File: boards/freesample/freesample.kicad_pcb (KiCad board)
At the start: 8 copper layers, 576 parts, among them J1 SMA, J10 XILINX_JTAG, J11 SMA, J12 SMA, J13 SMA, J14 SMA, J15 SMA, J16 SMA, J17 SMA, J18 SMA, J19 JUMPER, J2 BARREL, J20 JUMPER, J21 JUMPER, J22 SMA, J23 SMA, J24 SMA, J25 SMA, J26 PMOD_HOST, J3 SMA, J4 SMA, J5 SMA, J6 XILINX_JTAG, J7 CONN_INTEGRALSTICK_FPGA_HOST, J8 CONN_INTEGRALSTICK_MCU_HOST, J9 0826-1G1T-23-F, M1 TRACEPAD, M2 LOGO1, M3 LOGO2, M4 LOGO3, M5 LOGO4, M6 LOGO5, M7 LOGO6, Q1 SSM6N58NU, U1 HMC675LP3E, U10 PI6C59S6005, U11 PI6C59S6005, U12 PI6C59S6005, U13 SIP32408, U14 LMK04806, U15 ASG-D-V-A-125.000MHZ, U16 HMC856, U17 NB6L295, U18 PI6C59S6005, U19 NB7V52MMNG, U2 HMC675LP3E, U20 NB7V52MMNG, U21 NB7V52MMNG, U22 PI6C59S6005, U26 MCP1755ST-5002E/MC, U27 LM27761, U28 ADP1763Z-1.0, U29 ADP1763Z-1.0, U3 PI6C59S6005, U30 OKL-T/3-W12P-C, U31 ADP1741, U32 OKL-T/3-W12P-C, U33 ADP1741, U34 ADP1741, U35 OKL-T/3-W12P-C, U36 OKL-T/3-W12P-C, U37 LM27761, U38 OKL-T/3-W12P-C, U39 LM27761, U4 LTC2664CUH-16#PBF, U40 DS25BR150, U41 DS25BR150, U42 ADP1741, U43 ADP1741, U5 TLK10232, U6 LMK61PD0A2, U7 PI6C59S6005, U8 HMC675LP3E, U9 HMC675LP3E

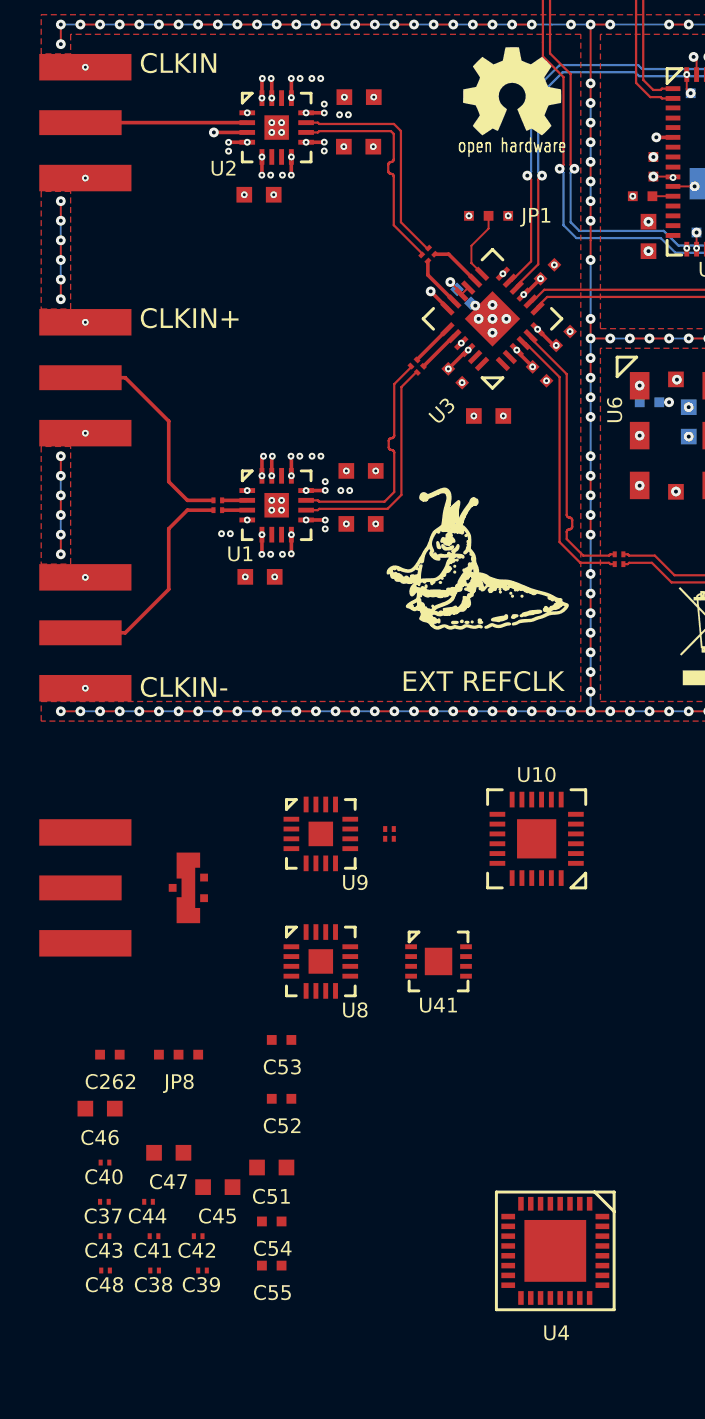
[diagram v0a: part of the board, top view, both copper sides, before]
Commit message: Continued layout on level trigger subsystem
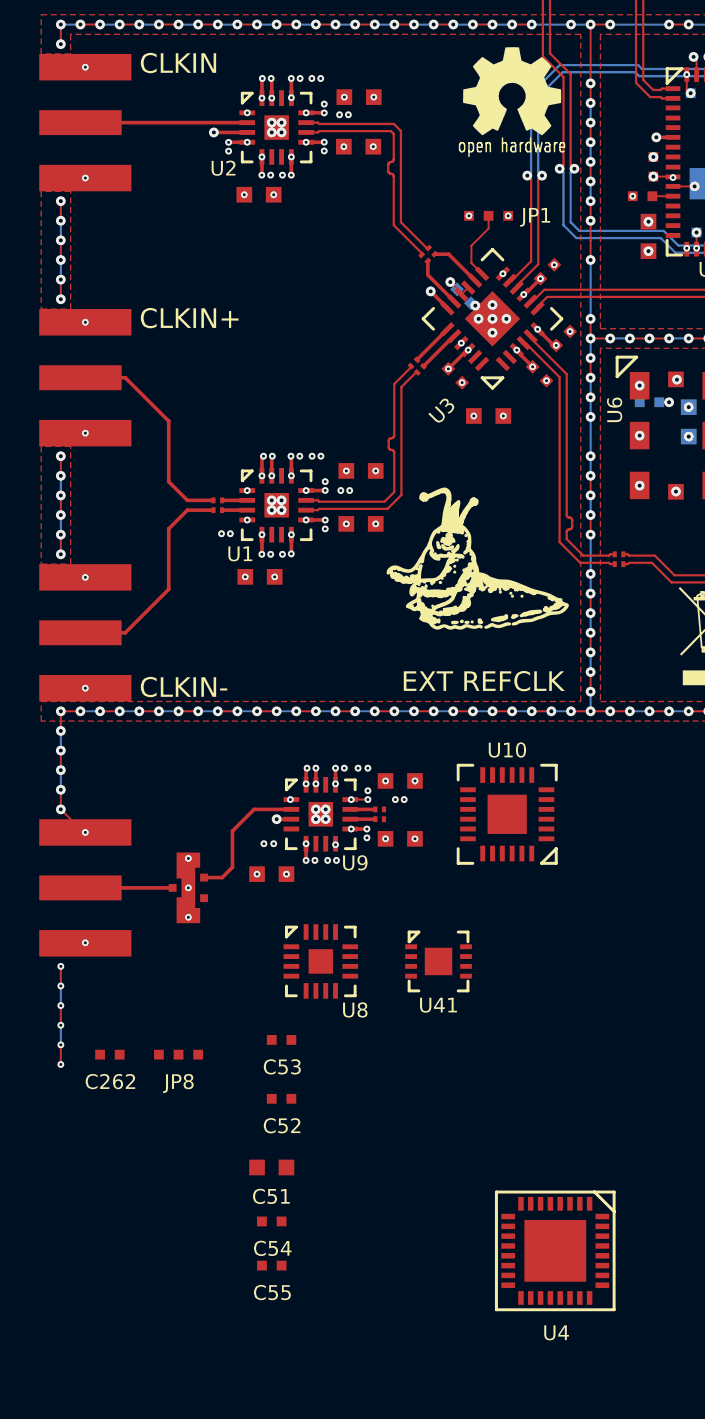
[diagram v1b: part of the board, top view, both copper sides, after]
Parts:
- moved C48 27.7 mm to (29.8, 157.9)
- moved C38 26.5 mm to (32.6, 159.3), turned to 90 degrees
- moved C39 26.5 mm to (31.2, 157.9)
- moved C42 25.3 mm to (32.4, 157.9)
- moved C44 24.2 mm to (34.3, 159.5)
- moved C41 23.2 mm to (32.6, 161.2), turned to 270 degrees
- moved C45 22.7 mm to (34.3, 158.6)
- moved C43 22.4 mm to (30.8, 162.6)
- moved C37 20.1 mm to (27.6, 161.8), turned to 180 degrees
- moved C47 19.9 mm to (34.3, 161.5)
- moved C40 18.6 mm to (29.7, 162.6)
- moved C46 14.8 mm to (27.8, 163.3)
- moved U10 1.95 mm to (39.8, 160.2)
- moved C49 1.12 mm to (33.2, 160.0), turned to 180 degrees
- moved C50 1.12 mm to (33.2, 160.5), turned to 180 degrees
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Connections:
- U10 pad 23: /Level triggering/LTRIG_SAMPOUT_N -> (no net)
- U10 pad 24: /Level triggering/LTRIG_SAMPOUT_P -> (no net)
- U10 pad 4: (no net) -> /Level triggering/LTRIG_SAMPOUT_N
- U10 pad 5: (no net) -> /Level triggering/LTRIG_SAMPOUT_P
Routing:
- net /GND: track 565.4 -> 632.0 mm, vias 369 -> 400
- net /1V8: track 91.1 -> 141.5 mm, vias 23 -> 29
- net /REFCLK_SINGLE_VT: track 33.8 -> 52.6 mm
- net /LTRIG_VT: track 0.00 -> 18.0 mm, vias 0 -> 1
- net /3V3: track 46.6 -> 63.7 mm, vias 14 -> 21
- net /3V0_N: track 48.1 -> 63.3 mm, vias 16 -> 24
- net /LTRIG_DIN: track 0.00 -> 6.97 mm
- net /VIN: track 0.00 -> 4.70 mm
- net /Level triggering/LTRIG_P: track 0.00 -> 1.28 mm
- net /Level triggering/LTRIG_N: track 0.00 -> 1.25 mm

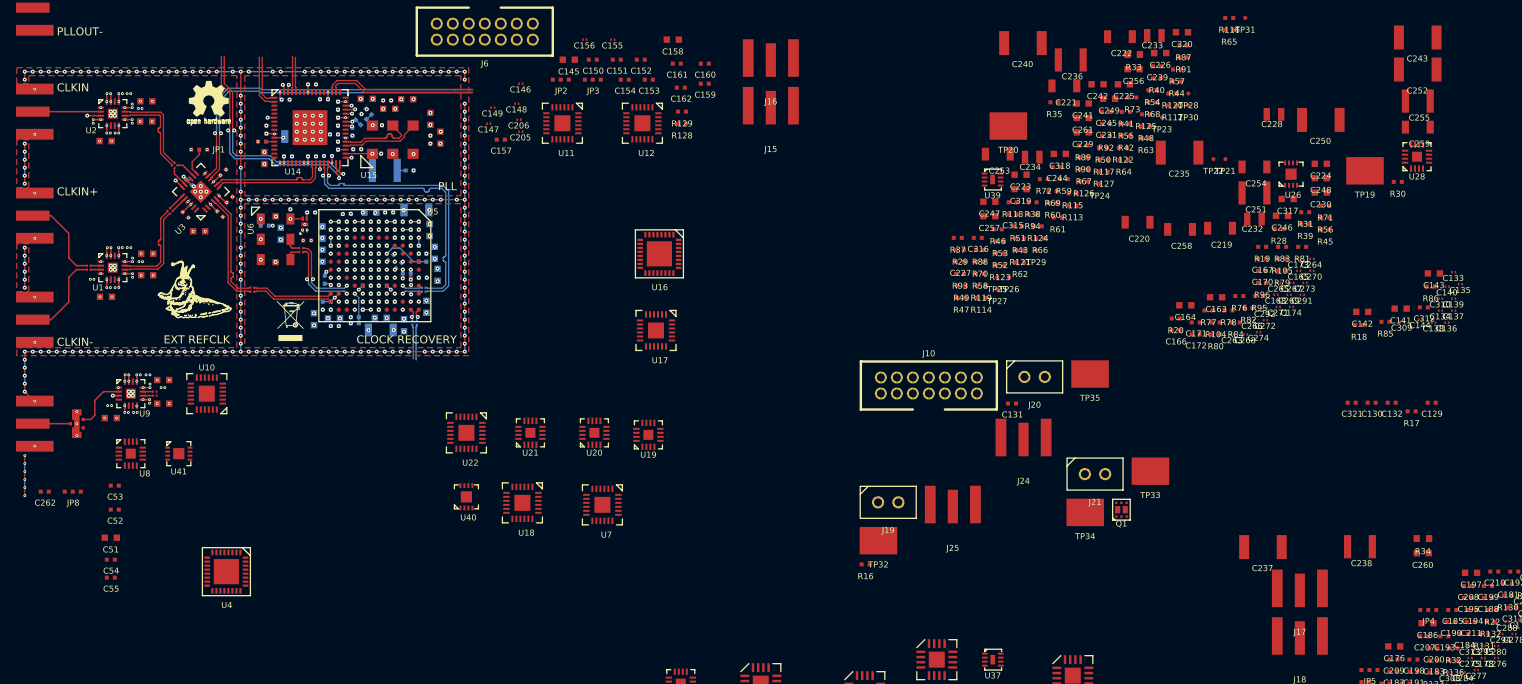
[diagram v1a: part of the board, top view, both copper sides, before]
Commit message: Finished initial layout of level trigger and ADC subsystems
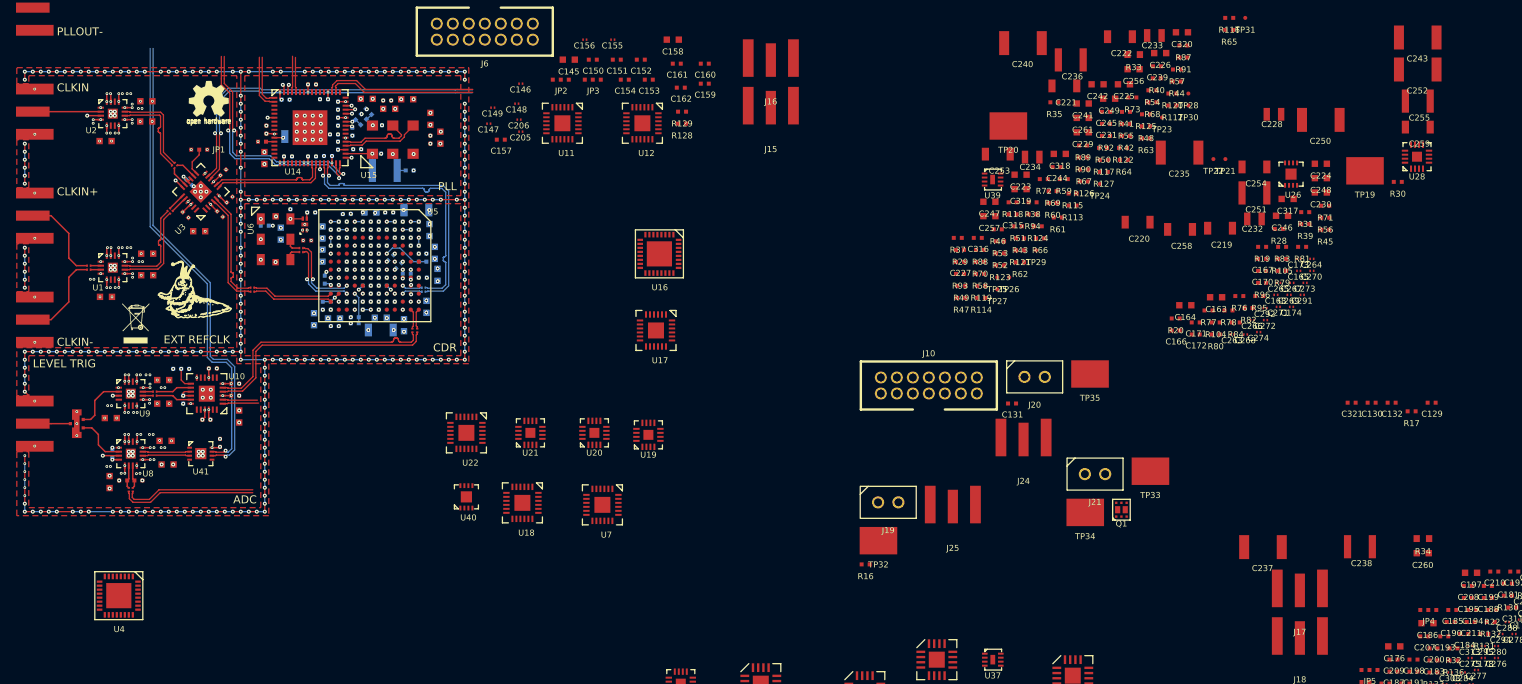
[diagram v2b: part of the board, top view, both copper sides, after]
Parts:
- C262, JP8, R18: moved to B.Cu
- C56, C57: moved to F.Cu
- moved C139 169.4 mm to (27.5, 169.3)
- moved C133 168.2 mm to (29.3, 170.2), turned to 180 degrees
- moved C135 166.3 mm to (31.2, 165.3)
- moved C310 165.2 mm to (30.5, 172.2), turned to 270 degrees
- moved C136 164.6 mm to (31.2, 170.2)
- moved C137 163.8 mm to (32.9, 168.5)
- moved R86 163.3 mm to (31.2, 171.1)
- moved C144 162.3 mm to (29.8, 165.3)
- moved C134 162.0 mm to (32.9, 167.0)
- moved C140 161.8 mm to (34.2, 167.0)
- moved C138 160.9 mm to (32.8, 165.3)
- moved C309 160.5 mm to (30.0, 172.2), turned to 270 degrees
- moved C143 160.1 mm to (34.9, 169.1)
- moved R85 159.0 mm to (29.3, 171.1)
- moved C142 158.0 mm to (27.6, 171.3), turned to 270 degrees
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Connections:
- U10 pad 1: /CDR/CDR_DIN_N -> /Level triggering/LTRIG_SAMPOUT_N
- U10 pad 2: /CDR/CDR_DIN_P -> /Level triggering/LTRIG_SAMPOUT_P
- U10 pad 4: /Level triggering/LTRIG_SAMPOUT_N -> /CDR/CDR_DIN_N
- U10 pad 5: /Level triggering/LTRIG_SAMPOUT_P -> /CDR/CDR_DIN_P
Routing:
- net /GND: track 632.0 -> 764.2 mm, vias 400 -> 481
- net /ADC_OUT_N: track 0.00 -> 58.7 mm, vias 0 -> 1
- net /ADC_OUT_P: track 0.00 -> 58.1 mm, vias 0 -> 1
- net /3V3_CLKBUF: track 46.4 -> 90.6 mm, vias 11 -> 23
- net /3V3: track 63.7 -> 96.4 mm, vias 21 -> 30
- net /CDR/CDR_DIN_P: track 4.32 -> 30.0 mm
- net /CDR/CDR_DIN_N: track 4.47 -> 29.9 mm
- net /1V0: track 43.8 -> 68.7 mm
- net /1V8: track 141.5 -> 163.1 mm, vias 29 -> 35
- net /3V0_N: track 63.3 -> 81.3 mm, vias 24 -> 32
- net /ADC/ADC_LE_N: track 0.00 -> 17.1 mm
- net /ADC/ADC_LE_P: track 0.00 -> 16.4 mm
- net /ADC_VT: track 0.00 -> 10.2 mm, vias 0 -> 1
- net /ADC_DIN: track 0.00 -> 6.44 mm
- net /ADC/ADC_CML_P: track 0.00 -> 5.91 mm
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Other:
- board text added: "ADC"
- board text added: "CDR"
- board text added: "LEVEL TRIG"
- board text removed: "CLOCK RECOVERY"
